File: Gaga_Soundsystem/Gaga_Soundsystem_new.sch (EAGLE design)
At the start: 16 parts, among them IC1 TUSB2046VF, Q2 6MHZ

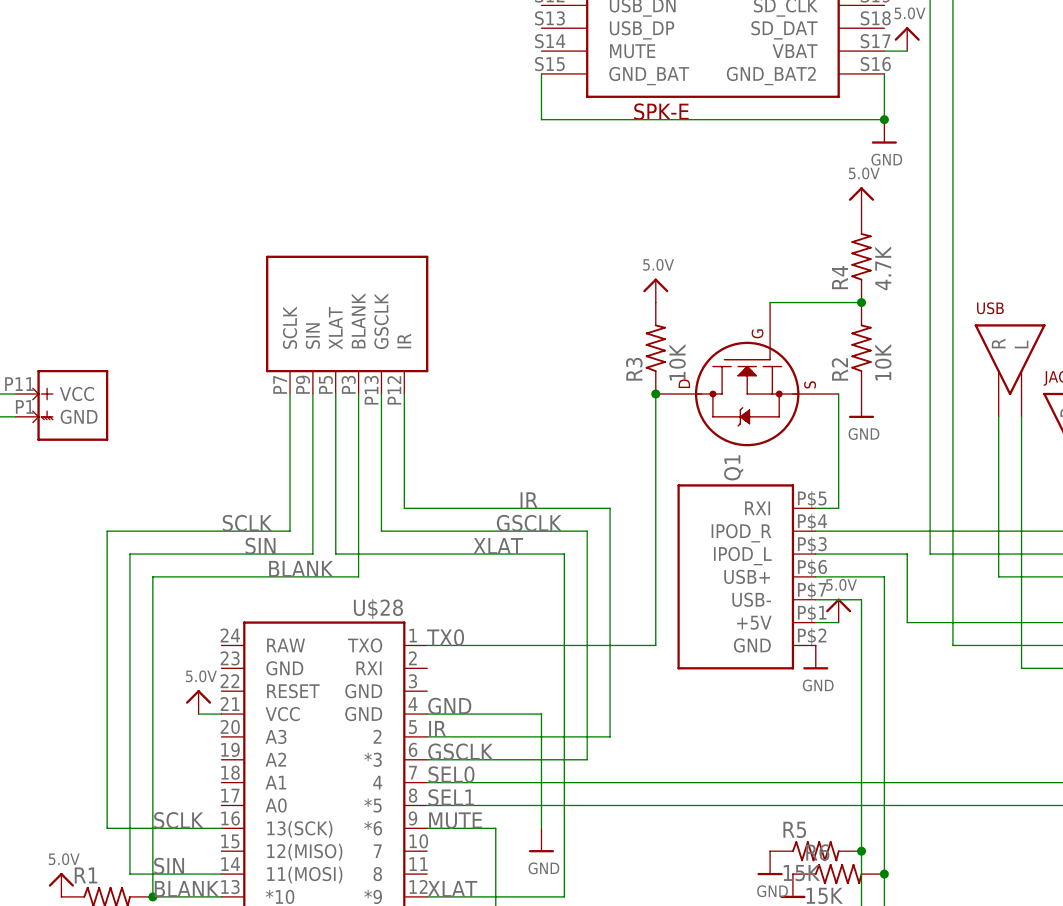
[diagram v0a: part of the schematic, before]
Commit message: resistor to smd and add 3.3v
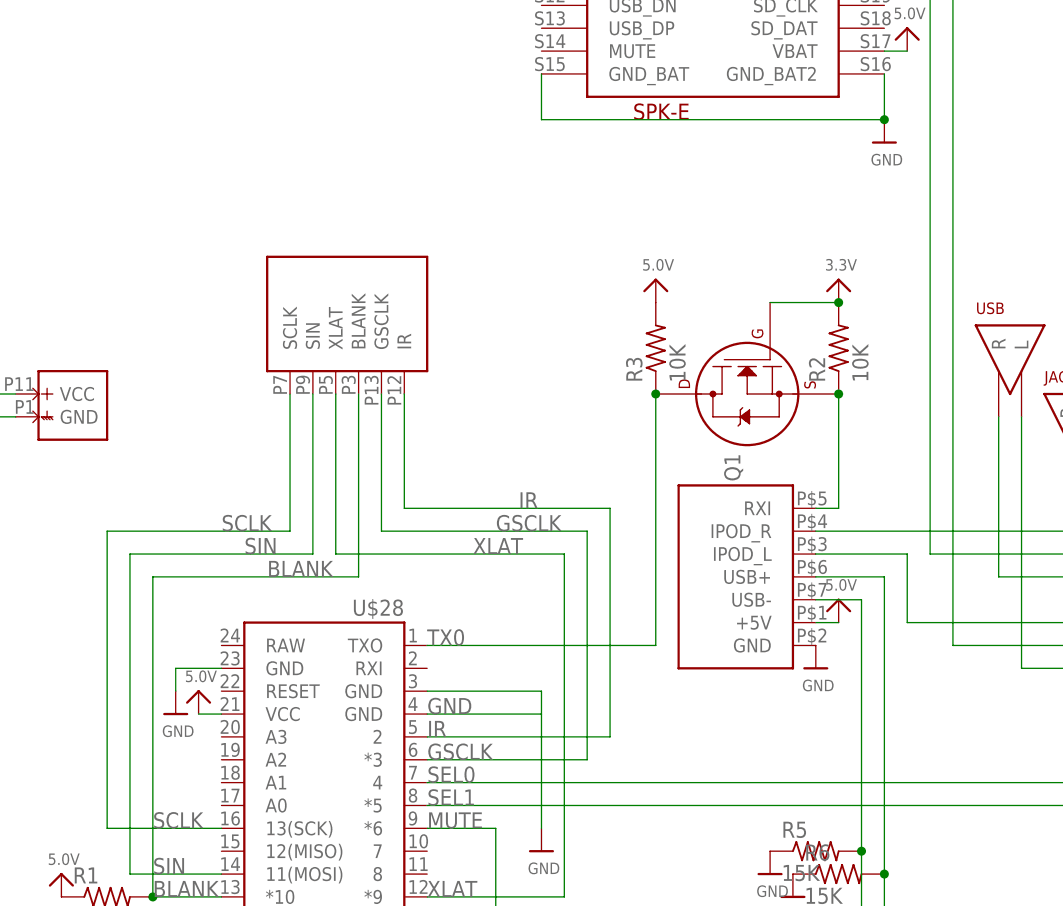
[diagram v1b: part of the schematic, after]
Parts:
- removed R4: 4.7K, resistor:R-US_0207/7
- R2: device resistor:R-US_0207/7 -> resistor:R-US_M0805
- R3: device resistor:R-US_0207/7 -> resistor:R-US_R0805
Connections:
- removed net N$4: Q1.G, R2.2, R4.1
- net 3.3V: now also Q1.G, R2.2
- net 5.0V: no longer R4.2
- net GND: now also U$28.GND@1, U$28.GND@2; no longer R2.1
- net N$1: now also R2.1
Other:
- moved on the sheet: R2
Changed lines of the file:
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@@
 <part name="U$28" library="SparkFun-Boards" deviceset="ARDUINO_PRO_MICRO" device=""/>
 <part name="Q1" library="transistors" deviceset="2N700*" device="_TO92" technology="0"/>
-<part name="R2" library="resistor" deviceset="R-US_" device="0207/7" value="10K"/>
-<part name="R3" library="resistor" deviceset="R-US_" device="0207/7" value="10K"/>
+<part name="R2" library="resistor" deviceset="R-US_" device="M0805" value="10K"/>
+<part name="R3" library="resistor" deviceset="R-US_" device="R0805" value="10K"/>
 <part name="U$2" library="microbuilder" deviceset="5.0V" device=""/>
-<part name="U$4" library="microbuilder" deviceset="GND" device=""/>
-<part name="R4" library="resistor" deviceset="R-US_" device="0207/7" value="4.7K"/>
-<part name="U$6" library="microbuilder" deviceset="5.0V" device=""/>
 <part name="IC1" library="jt-texas" deviceset="TUSB2046" device="VF"/>
 <part name="U$10" library="microbuilder" deviceset="GND" device=""/>
@@
 <part name="U$25" library="microbuilder" deviceset="3.3V" device=""/>
 <part name="U$26" library="microbuilder" deviceset="GND" device=""/>
+<part name="U$29" library="microbuilder" deviceset="GND" device=""/>
+<part name="U$6" library="microbuilder" deviceset="3.3V" device=""/>
 </parts>
 <sheets>
@@
 <instance part="U$28" gate="G$1" x="17.78" y="20.32" rot="MR0"/>
 <instance part="Q1" gate="G$1" x="63.5" y="63.5" rot="MR270"/>
-<instance part="R2" gate="G$1" x="76.2" y="68.58" rot="R90"/>
+<instance part="R2" gate="G$1" x="73.66" y="68.58" rot="R90"/>
 <instance part="R3" gate="G$1" x="53.34" y="68.58" rot="R90"/>
 <instance part="U$2" gate="G$1" x="53.34" y="76.2"/>
-<instance part="U$4" gate="G$1" x="76.2" y="60.96"/>
-<instance part="R4" gate="G$1" x="76.2" y="78.74" rot="R90"/>
-<instance part="U$6" gate="G$1" x="76.2" y="86.36"/>
 <instance part="IC1" gate="G$1" x="104.14" y="-20.32" rot="MR0"/>
 <instance part="U$10" gate="G$1" x="104.14" y="-63.5" rot="MR0"/>
@@
 <instance part="U$25" gate="G$1" x="129.54" y="-30.48"/>
 <instance part="U$26" gate="G$1" x="129.54" y="-25.4" rot="MR0"/>
+<instance part="U$29" gate="G$1" x="0" y="27.94"/>
+<instance part="U$6" gate="G$1" x="73.66" y="76.2"/>
 </instances>
 <busses>
@@
 <label x="27.94" y="27.94" size="1.778" layer="95"/>
 <pinref part="U$28" gate="G$1" pin="GND"/>
+<pinref part="U$28" gate="G$1" pin="GND@1"/>
+<wire x1="27.94" y1="30.48" x2="40.64" y2="30.48" width="0.1524" layer="91"/>
+<wire x1="40.64" y1="30.48" x2="40.64" y2="27.94" width="0.1524" layer="91"/>
 </segment>
 <segment>
@@
 </segment>
 <segment>
-<pinref part="R2" gate="G$1" pin="1"/>
-<pinref part="U$4" gate="G$1" pin="GND"/>
-</segment>
-<segment>
 <pinref part="IC1" gate="G$1" pin="GND@7"/>
 <pinref part="IC1" gate="G$1" pin="GND@28"/>
@@
 <wire x1="127" y1="-22.86" x2="129.54" y2="-22.86" width="0.1524" layer="91"/>
 </segment>
+<segment>
+<pinref part="U$28" gate="G$1" pin="GND@2"/>
+<wire x1="5.08" y1="33.02" x2="0" y2="33.02" width="0.1524" layer="91"/>
+<wire x1="0" y1="33.02" x2="0" y2="30.48" width="0.1524" layer="91"/>
+<pinref part="U$29" gate="G$1" pin="GND"/>
+</segment>
 </net>
 <net name="5.0V" class="0">
@@
 <pinref part="R3" gate="G$1" pin="2"/>
 <pinref part="U$2" gate="G$1" pin="5.0V"/>
-</segment>
-<segment>
-<pinref part="R4" gate="G$1" pin="2"/>
-<pinref part="U$6" gate="G$1" pin="5.0V"/>
 </segment>
 </net>
@@
 <wire x1="73.66" y1="63.5" x2="73.66" y2="50.8" width="0.1524" layer="91"/>
 <wire x1="73.66" y1="50.8" x2="71.12" y2="50.8" width="0.1524" layer="91"/>
-</segment>
-</net>
-<net name="N$4" class="0">
-<segment>
-<pinref part="Q1" gate="G$1" pin="G"/>
-<pinref part="R2" gate="G$1" pin="2"/>
-<wire x1="66.04" y1="73.66" x2="76.2" y2="73.66" width="0.1524" layer="91"/>
-<pinref part="R4" gate="G$1" pin="1"/>
-<junction x="76.2" y="73.66"/>
+<pinref part="R2" gate="G$1" pin="1"/>
+<junction x="73.66" y="63.5"/>
 </segment>
 </net>
@@
 <wire x1="127" y1="-33.02" x2="129.54" y2="-33.02" width="0.1524" layer="91"/>
 </segment>
-</net>
+<segment>
+<pinref part="Q1" gate="G$1" pin="G"/>
+<pinref part="R2" gate="G$1" pin="2"/>
+<wire x1="66.04" y1="73.66" x2="73.66" y2="73.66" width="0.1524" layer="91"/>
+<pinref part="U$6" gate="G$1" pin="3.3V"/>
+<junction x="73.66" y="73.66"/>
+</segment>
+</net>

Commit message: alt
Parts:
- added IC2: LM358, SparkFun-AnalogIC:LM358
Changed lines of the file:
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@@
 <grid distance="0.1" unitdist="inch" unit="inch" style="lines" multiple="1" display="no" altdistance="0.01" altunitdist="inch" altunit="inch"/>
 <layers>
-<layer number="1" name="Top" color="4" fill="1" visible="yes" active="no"/>
-<layer number="2" name="Route2" color="1" fill="3" visible="yes" active="no"/>
-<layer number="3" name="Route3" color="4" fill="3" visible="yes" active="no"/>
-<layer number="4" name="Route4" color="1" fill="4" visible="yes" active="no"/>
-<layer number="5" name="Route5" color="4" fill="4" visible="yes" active="no"/>
-<layer number="6" name="Route6" color="1" fill="8" visible="yes" active="no"/>
-<layer number="7" name="Route7" color="4" fill="8" visible="yes" active="no"/>
-<layer number="8" name="Route8" color="1" fill="2" visible="yes" active="no"/>
-<layer number="9" name="Route9" color="4" fill="2" visible="yes" active="no"/>
-<layer number="10" name="Route10" color="1" fill="7" visible="yes" active="no"/>
-<layer number="11" name="Route11" color="4" fill="7" visible="yes" active="no"/>
-<layer number="12" name="Route12" color="1" fill="5" visible="yes" active="no"/>
-<layer number="13" name="Route13" color="4" fill="5" visible="yes" active="no"/>
-<layer number="14" name="Route14" color="1" fill="6" visible="yes" active="no"/>
-<layer number="15" name="Route15" color="4" fill="6" visible="yes" active="no"/>
-<layer number="16" name="Bottom" color="1" fill="1" visible="yes" active="no"/>
-<layer number="17" name="Pads" color="2" fill="1" visible="yes" active="no"/>
-<layer number="18" name="Vias" color="2" fill="1" visible="yes" active="no"/>
-<layer number="19" name="Unrouted" color="6" fill="1" visible="yes" active="no"/>
-<layer number="20" name="Dimension" color="15" fill="1" visible="yes" active="no"/>
-<layer number="21" name="tPlace" color="7" fill="1" visible="yes" active="no"/>
-<layer number="22" name="bPlace" color="7" fill="1" visible="yes" active="no"/>
-<layer number="23" name="tOrigins" color="15" fill="1" visible="yes" active="no"/>
-<layer number="24" name="bOrigins" color="15" fill="1" visible="yes" active="no"/>
-<layer number="25" name="tNames" color="7" fill="1" visible="yes" active="no"/>
-<layer number="26" name="bNames" color="7" fill="1" visible="yes" active="no"/>
-<layer number="27" name="tValues" color="7" fill="1" visible="yes" active="no"/>
-<layer number="28" name="bValues" color="7" fill="1" visible="yes" active="no"/>
+<layer number="1" name="Top" color="4" fill="1" visible="no" active="no"/>
+<layer number="2" name="Route2" color="1" fill="3" visible="no" active="no"/>
+<layer number="3" name="Route3" color="4" fill="3" visible="no" active="no"/>
+<layer number="4" name="Route4" color="1" fill="4" visible="no" active="no"/>
+<layer number="5" name="Route5" color="4" fill="4" visible="no" active="no"/>
+<layer number="6" name="Route6" color="1" fill="8" visible="no" active="no"/>
+<layer number="7" name="Route7" color="4" fill="8" visible="no" active="no"/>
+<layer number="8" name="Route8" color="1" fill="2" visible="no" active="no"/>
+<layer number="9" name="Route9" color="4" fill="2" visible="no" active="no"/>
+<layer number="10" name="Route10" color="1" fill="7" visible="no" active="no"/>
+<layer number="11" name="Route11" color="4" fill="7" visible="no" active="no"/>
+<layer number="12" name="Route12" color="1" fill="5" visible="no" active="no"/>
+<layer number="13" name="Route13" color="4" fill="5" visible="no" active="no"/>
+<layer number="14" name="Route14" color="1" fill="6" visible="no" active="no"/>
+<layer number="15" name="Route15" color="4" fill="6" visible="no" active="no"/>
+<layer number="16" name="Bottom" color="1" fill="1" visible="no" active="no"/>
+<layer number="17" name="Pads" color="2" fill="1" visible="no" active="no"/>
+<layer number="18" name="Vias" color="2" fill="1" visible="no" active="no"/>
+<layer number="19" name="Unrouted" color="6" fill="1" visible="no" active="no"/>
+<layer number="20" name="Dimension" color="15" fill="1" visible="no" active="no"/>
+<layer number="21" name="tPlace" color="7" fill="1" visible="no" active="no"/>
+<layer number="22" name="bPlace" color="7" fill="1" visible="no" active="no"/>
+<layer number="23" name="tOrigins" color="15" fill="1" visible="no" active="no"/>
+<layer number="24" name="bOrigins" color="15" fill="1" visible="no" active="no"/>
+<layer number="25" name="tNames" color="7" fill="1" visible="no" active="no"/>
+<layer number="26" name="bNames" color="7" fill="1" visible="no" active="no"/>
+<layer number="27" name="tValues" color="7" fill="1" visible="no" active="no"/>
+<layer number="28" name="bValues" color="7" fill="1" visible="no" active="no"/>
 <layer number="29" name="tStop" color="7" fill="3" visible="no" active="no"/>
 <layer number="30" name="bStop" color="7" fill="6" visible="no" active="no"/>
@@
 <layer number="35" name="tGlue" color="7" fill="4" visible="no" active="no"/>
 <layer number="36" name="bGlue" color="7" fill="5" visible="no" active="no"/>
-<layer number="37" name="tTest" color="7" fill="1" visible="yes" active="no"/>
-<layer number="38" name="bTest" color="7" fill="1" visible="yes" active="no"/>
+<layer number="37" name="tTest" color="7" fill="1" visible="no" active="no"/>
+<layer number="38" name="bTest" color="7" fill="1" visible="no" active="no"/>
 <layer number="39" name="tKeepout" color="4" fill="11" visible="no" active="no"/>
 <layer number="40" name="bKeepout" color="1" fill="11" visible="no" active="no"/>
@@
 <layer number="44" name="Drills" color="7" fill="1" visible="no" active="no"/>
 <layer number="45" name="Holes" color="7" fill="1" visible="no" active="no"/>
-<layer number="46" name="Milling" color="3" fill="1" visible="yes" active="no"/>
-<layer number="47" name="Measures" color="7" fill="1" visible="yes" active="no"/>
-<layer number="48" name="Document" color="7" fill="1" visible="yes" active="no"/>
-<layer number="49" name="Reference" color="7" fill="1" visible="yes" active="no"/>
-<layer number="50" name="dxf" color="7" fill="1" visible="yes" active="no"/>
-<layer number="51" name="tDocu" color="7" fill="1" visible="yes" active="no"/>
-<layer number="52" name="bDocu" color="7" fill="1" visible="yes" active="no"/>
-<layer number="53" name="tGND_GNDA" color="7" fill="9" visible="yes" active="no"/>
-<layer number="54" name="bGND_GNDA" color="1" fill="9" visible="yes" active="no"/>
-<layer number="56" name="wert" color="7" fill="1" visible="yes" active="no"/>
+<layer number="46" name="Milling" color="3" fill="1" visible="no" active="no"/>
+<layer number="47" name="Measures" color="7" fill="1" visible="no" active="no"/>
+<layer number="48" name="Document" color="7" fill="1" visible="no" active="no"/>
+<layer number="49" name="Reference" color="7" fill="1" visible="no" active="no"/>
+<layer number="50" name="dxf" color="7" fill="1" visible="no" active="no"/>
+<layer number="51" name="tDocu" color="7" fill="1" visible="no" active="no"/>
+<layer number="52" name="bDocu" color="7" fill="1" visible="no" active="no"/>
+<layer number="53" name="tGND_GNDA" color="7" fill="9" visible="no" active="no"/>
+<layer number="54" name="bGND_GNDA" color="1" fill="9" visible="no" active="no"/>
+<layer number="56" name="wert" color="7" fill="1" visible="no" active="no"/>
 <layer number="91" name="Nets" color="2" fill="1" visible="yes" active="yes"/>
 <layer number="92" name="Busses" color="1" fill="1" visible="yes" active="yes"/>
@@
 <layer number="151" name="HeatSink" color="7" fill="1" visible="yes" active="yes"/>
 <layer number="152" name="_bDocu" color="7" fill="1" visible="yes" active="yes"/>
+<layer number="199" name="Contour" color="7" fill="1" visible="yes" active="yes"/>
 <layer number="200" name="200bmp" color="1" fill="10" visible="yes" active="yes"/>
 <layer number="201" name="201bmp" color="2" fill="10" visible="yes" active="yes"/>
@@
 <part name="U$29" library="microbuilder" deviceset="GND" device=""/>
 <part name="U$6" library="microbuilder" deviceset="3.3V" device=""/>
+<part name="IC2" library="SparkFun-AnalogIC" deviceset="LM358" device=""/>
 </parts>
 <sheets>
@@
 <instance part="U$29" gate="G$1" x="0" y="27.94"/>
 <instance part="U$6" gate="G$1" x="73.66" y="76.2"/>
+<instance part="IC2" gate="G1" x="177.8" y="91.44"/>
+<instance part="IC2" gate="G2" x="213.36" y="91.44"/>
 </instances>
 <busses>
